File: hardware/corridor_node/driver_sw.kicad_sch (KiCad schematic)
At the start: 6 parts, among them U2 SD3361

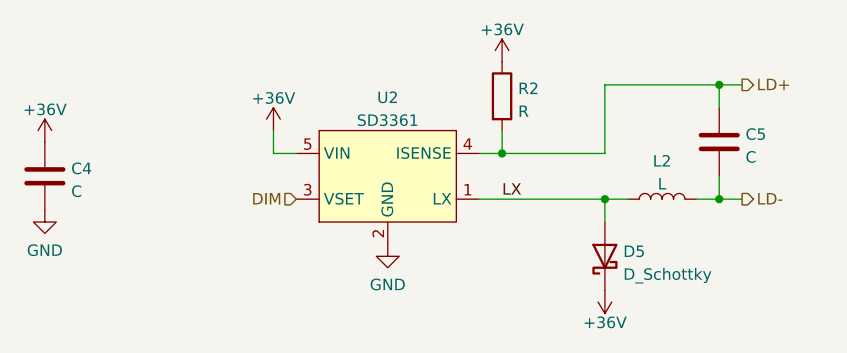
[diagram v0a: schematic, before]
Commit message: led balance and corridor ready
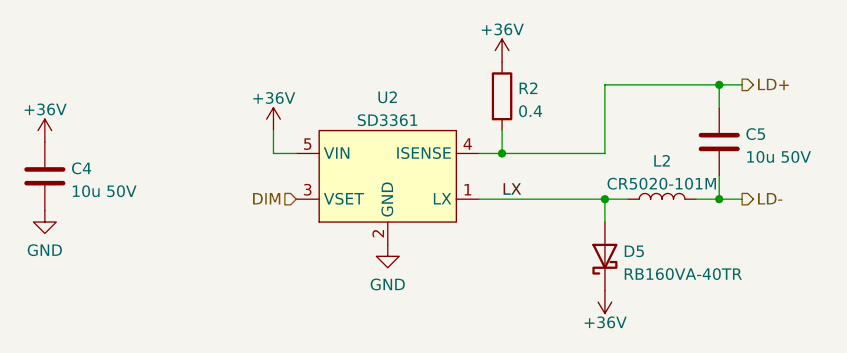
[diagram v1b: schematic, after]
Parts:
- C4, C5: value C -> 10u 50V; LCSC Part # (none) -> C440198
- D5: value D_Schottky -> RB160VA-40TR; LCSC Part # (none) -> C425675
- L2: value L -> CR5020-101M; LCSC Part # (none) -> C7588705
- R2: value R -> 0.4; LCSC Part # (none) -> C175713
- U2: LCSC Part # (none) -> C521345
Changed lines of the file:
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@@
+      (effects (font (size 1.27 1.27)) hide)
+    )
+    (property "LCSC Part #" "C521345" (at 139.7 88.9 0)
       (effects (font (size 1.27 1.27)) hide)
     )
@@
       (effects (font (size 1.27 1.27)) (justify right))
     )
-    (property "Value" "D_Schottky" (at 165.862 99.8097 90)
+    (property "Value" "RB160VA-40TR" (at 165.862 99.8097 90)
       (effects (font (size 1.27 1.27)) (justify right))
     )
@@
       (effects (font (size 1.27 1.27)) hide)
     )
-    (property "Datasheet" "~" (at 163.83 97.79 0)
+    (property "Datasheet" "https://datasheet.lcsc.com/lcsc/1912111437_ROHM-Semicon-RB160VA-40TR_C425675.pdf" (at 163.83 97.79 0)
+      (effects (font (size 1.27 1.27)) hide)
+    )
+    (property "LCSC Part #" "C425675" (at 163.83 97.79 0)
       (effects (font (size 1.27 1.27)) hide)
     )
@@
       (effects (font (size 1.27 1.27)) (justify left))
     )
-    (property "Value" "R" (at 154.178 81.7122 0)
+    (property "Value" "0.4" (at 154.178 81.7122 0)
       (effects (font (size 1.27 1.27)) (justify left))
     )
@@
       (effects (font (size 1.27 1.27)) hide)
     )
+    (property "LCSC Part #" "C175713" (at 152.4 80.01 0)
+      (effects (font (size 1.27 1.27)) hide)
+    )
     (pin "1")
     (pin "2")
@@
       (effects (font (size 1.27 1.27)))
     )
-    (property "Value" "L" (at 170.18 89.7691 90)
+    (property "Value" "CR5020-101M" (at 170.18 89.7691 90)
       (effects (font (size 1.27 1.27)))
     )
@@
     )
     (property "Datasheet" "~" (at 170.18 91.44 0)
+      (effects (font (size 1.27 1.27)) hide)
+    )
+    (property "LCSC Part #" "C7588705" (at 170.18 91.44 0)
       (effects (font (size 1.27 1.27)) hide)
     )
@@
       (effects (font (size 1.27 1.27)) (justify left))
     )
-    (property "Value" "C" (at 179.451 86.7922 0)
+    (property "Value" "10u 50V" (at 179.451 86.7922 0)
       (effects (font (size 1.27 1.27)) (justify left))
     )
@@
       (effects (font (size 1.27 1.27)) hide)
     )
+    (property "LCSC Part #" "C440198" (at 176.53 85.09 0)
+      (effects (font (size 1.27 1.27)) hide)
+    )
     (pin "1")
     (pin "2")
@@
       (effects (font (size 1.27 1.27)) (justify left))
     )
-    (property "Value" "C" (at 104.521 90.6022 0)
+    (property "Value" "10u 50V" (at 104.521 90.6022 0)
       (effects (font (size 1.27 1.27)) (justify left))
     )
@@
       (effects (font (size 1.27 1.27)) hide)
     )
+    (property "LCSC Part #" "C440198" (at 101.6 88.9 0)
+      (effects (font (size 1.27 1.27)) hide)
+    )

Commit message: nightLight pcb files version upgrade
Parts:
- renumbered C4 to C2, C5 to C3, D5 to D4, L2 to L1, R2 to R1, U2 to U1
